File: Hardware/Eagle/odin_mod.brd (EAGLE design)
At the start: 21.4 x 22.8 mm, 36 parts

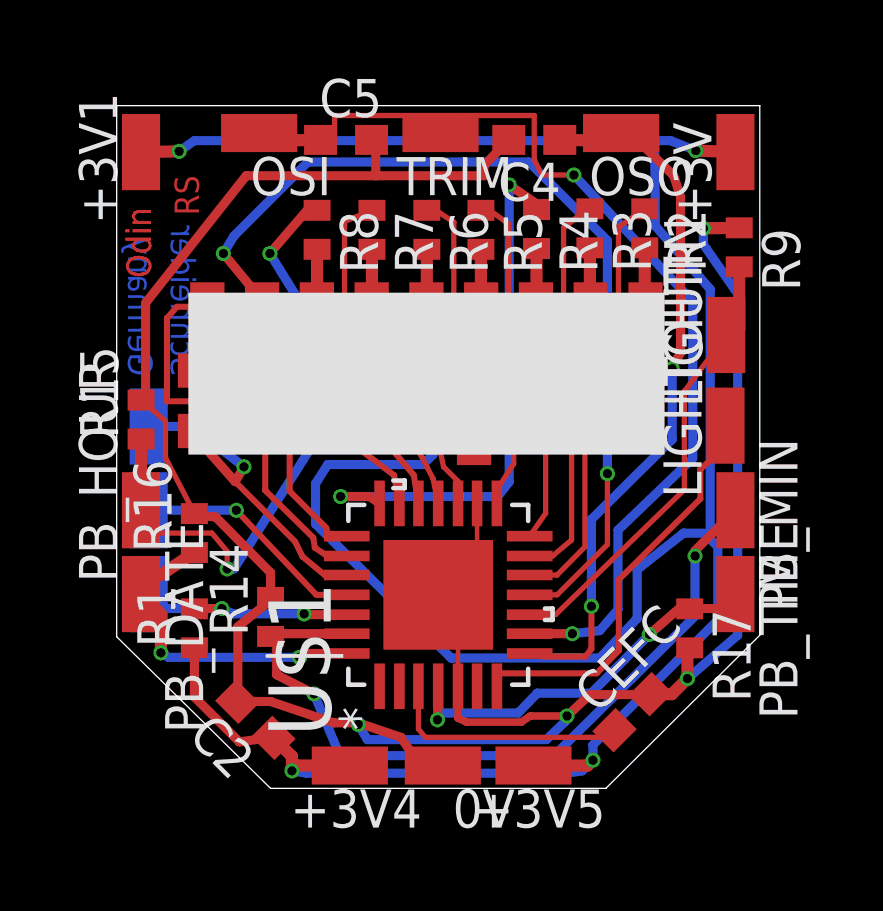
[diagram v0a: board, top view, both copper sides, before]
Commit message: Reworked layout for odin and loki boards.
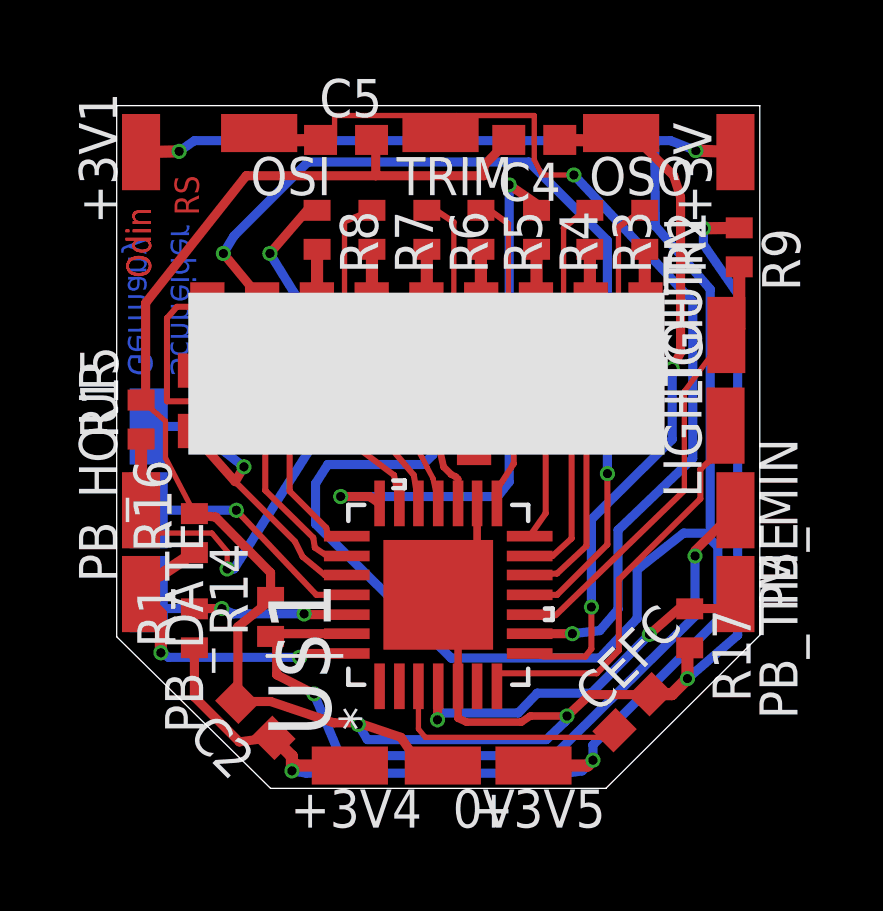
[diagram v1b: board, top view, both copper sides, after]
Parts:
- CEFC: value 4.7-10 uF -> 10 uF
- moved R2 0.05 mm to (17.6, 18.6)
- moved R3 0.05 mm to (15.7, 18.6)
